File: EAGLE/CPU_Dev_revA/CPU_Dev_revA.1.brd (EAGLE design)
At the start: 50.8 x 38.1 mm, 29 parts, among them J1 MICRO_USB_SMD, J2 HEADER_5PIN, J3 HEADER_2PIN, J4 HEADER_16PIN, J5 HEADER_16PIN, J6 HEADER_3PIN, SW1 RESET, U1 STM32L151C8T6, U2 3.3V LDO, Y1 16MHz

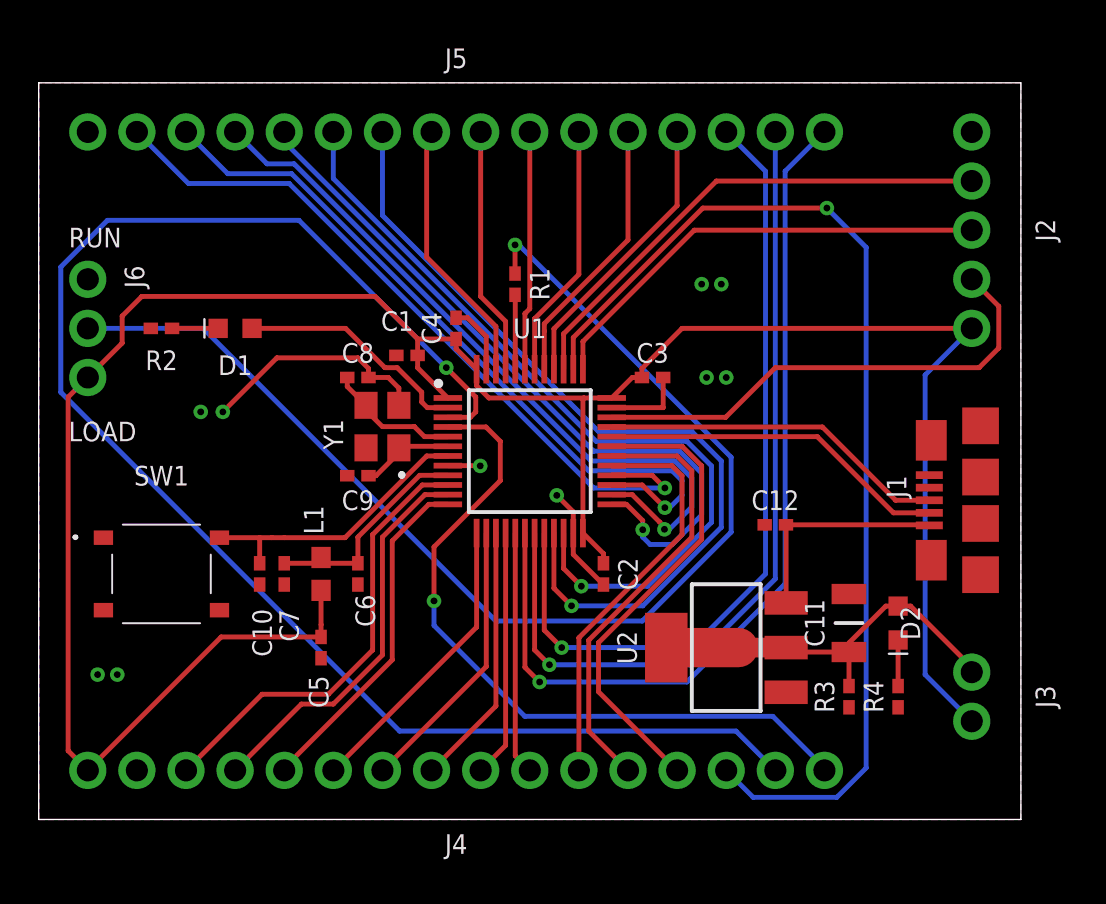
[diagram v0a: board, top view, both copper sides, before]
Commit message: CPU revB
Added CPU revB Eagle, gerber, BOM, and CPL files.
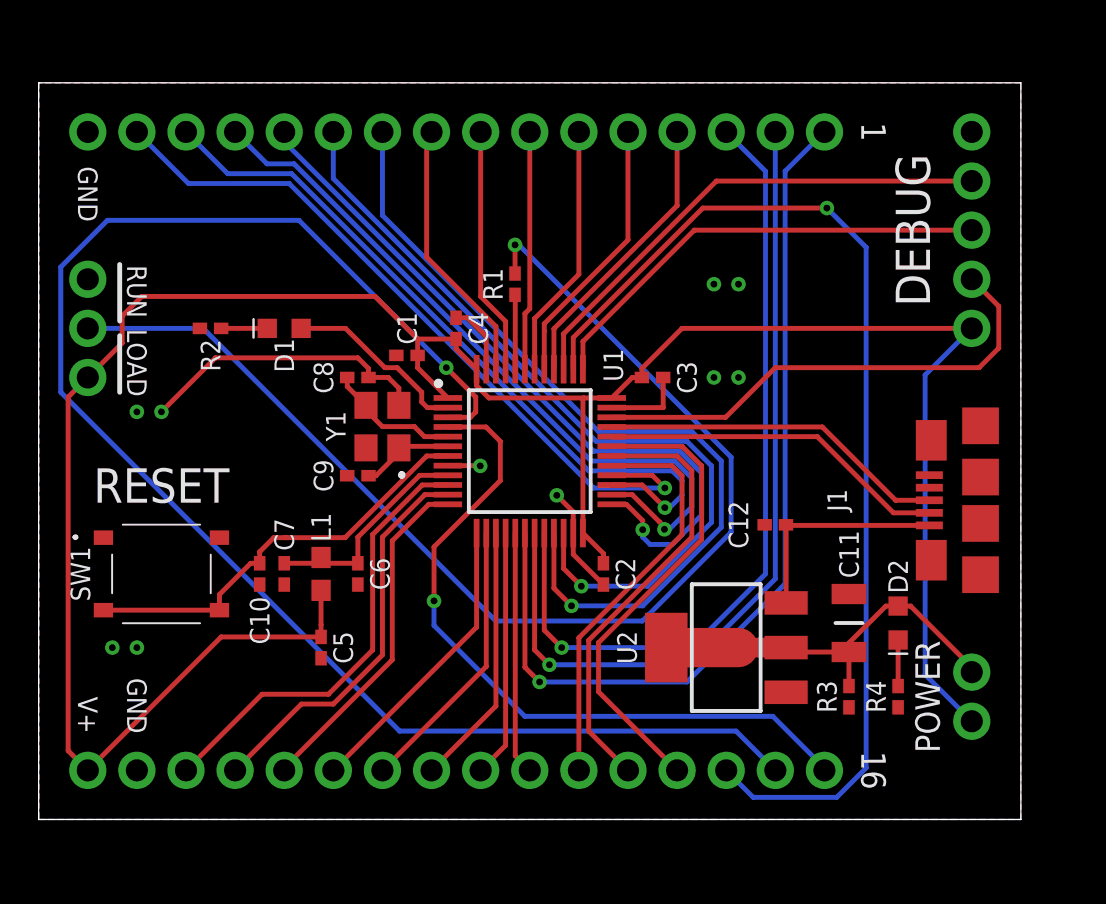
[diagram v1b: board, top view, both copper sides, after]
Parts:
- moved J1 2.90 mm to (47.3, 16.5)
- moved R2 2.54 mm to (8.89, 25.4)
- moved D1 2.54 mm to (12.7, 25.4)
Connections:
- net GND: now also SW1.B1
- net NRST: now also SW1.C1, SW1.D1; no longer SW1.B1
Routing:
- net NRST: track 14.9 -> 22.1 mm
- net GND: track 27.3 -> 30.4 mm
- net WKUP: track 12.1 -> 9.58 mm
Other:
- board text added: "1"
- board text added: "16"
- board text added: "CPU DEVELOPMENT BOARD revA.1"
- board text added: "DEBUG"
- board text added: "GND"
- board text added: "NSE LABS"
- board text added: "POWER"
- board text added: "RESET"
- board text added: "V+"
